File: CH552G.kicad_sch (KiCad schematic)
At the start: 13 parts, among them SW1 SW_SPST, SW2 SW_SPST, SW3 SW_SPST, SW4 SW_SPST, SW5 SW_SPST, SW6 SW_SPST, U1 CH552G

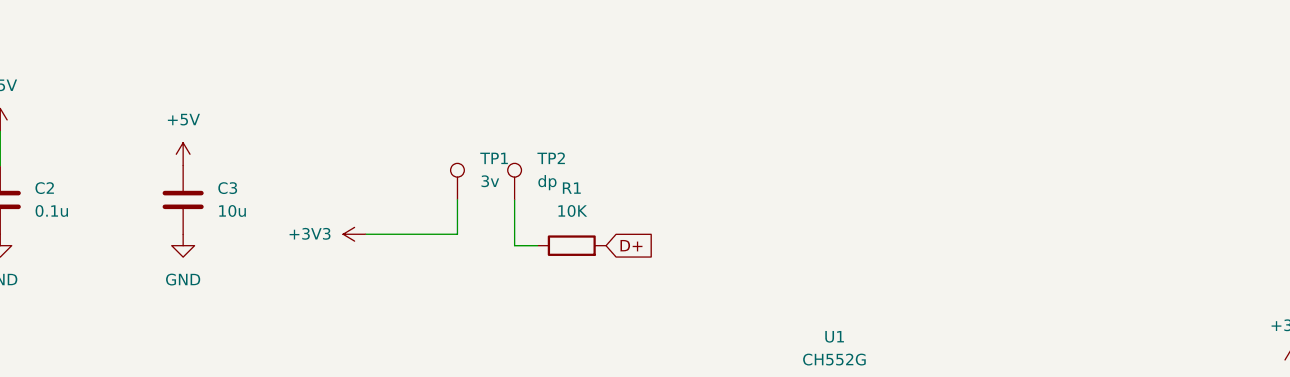
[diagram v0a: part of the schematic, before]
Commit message: updated titles and changes to wires
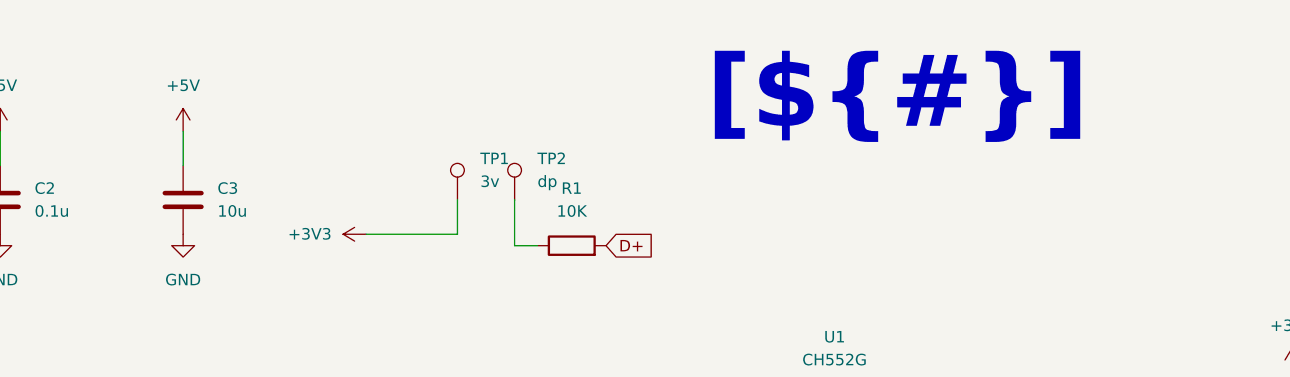
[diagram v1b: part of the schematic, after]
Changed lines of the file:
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@@
 	(generator_version "9.0")
 	(paper "A4")
+	(text_box "[${#}] ${TITLE}"
+		(exclude_from_sim no)
+		(at 82.55 16.002 0)
+		(size 130.81 12.7)
+		(margins 5.9999 5.9999 5.9999 5.9999)
+		(stroke
+			(width -0.0001)
+			(type default)
+		)
+		(fill
+			(type none)
+		)
+		(effects
+			(font
+				(face "Times New Roman")
+				(size 8 8)
+				(thickness 1.2)
+				(bold yes)
+				(color 162 22 34 1)
+			)
+		)
+	)
 	(junction
 		(at 35.56 27.94)
@@
 		(pts
 			(xy 40.64 135.89) (xy 54.61 135.89)
+		)
+		(stroke
+			(width 0)
+			(type default)
+		)
+	)
+	(wire
+		(pts
+			(xy 68.58 26.67) (xy 68.58 30.48)
 		)
 		(stroke
@@
 	(symbol
 		(lib_id "power:+5V")
-		(at 68.58 30.48 0)
+		(at 68.58 26.67 0)
 		(unit 1)
 		(exclude_from_sim no)
@@
 		(fields_autoplaced yes)
 		(property "Reference" "#PWR05"
-			(at 68.58 34.29 0)
+			(at 68.58 30.48 0)
 			(effects
 				(font
@@
 		)
 		(property "Value" "+5V"
-			(at 68.58 25.4 0)
+			(at 68.58 21.59 0)
 			(effects
 				(font
@@
 		)
 		(property "Footprint" ""
-			(at 68.58 30.48 0)
+			(at 68.58 26.67 0)
 			(effects
 				(font
@@
 		)
 		(property "Datasheet" ""
-			(at 68.58 30.48 0)
+			(at 68.58 26.67 0)
 			(effects
 				(font
@@
 		)
 		(property "Description" "Power symbol creates a global label with name \"+5V\""
-			(at 68.58 30.48 0)
-			(effects
-				(font
+			(at 68.58 26.67 0)
+			(effects
+				(font

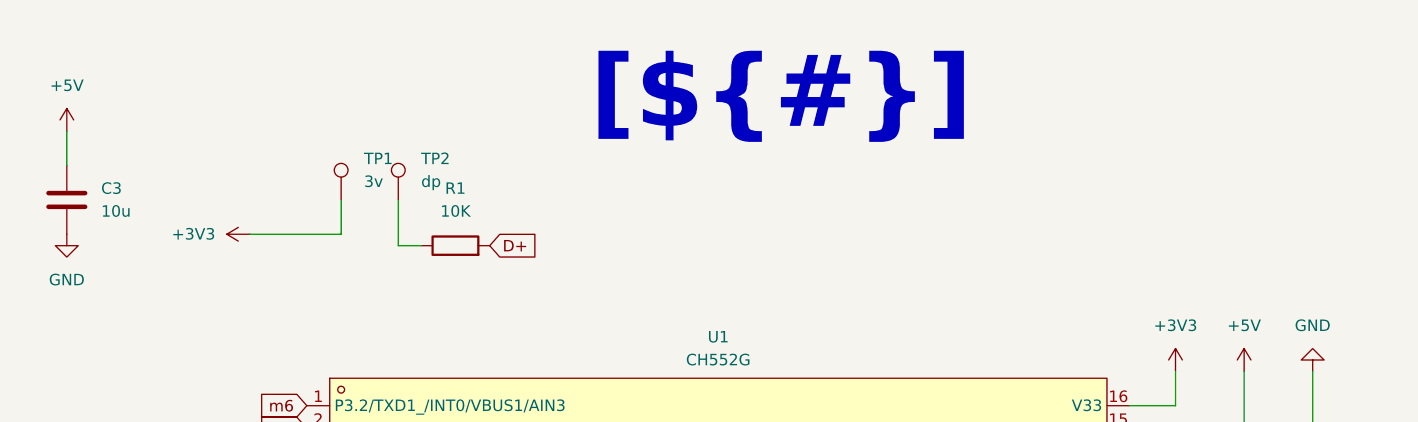
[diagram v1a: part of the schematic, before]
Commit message: updated titles and changes to wires
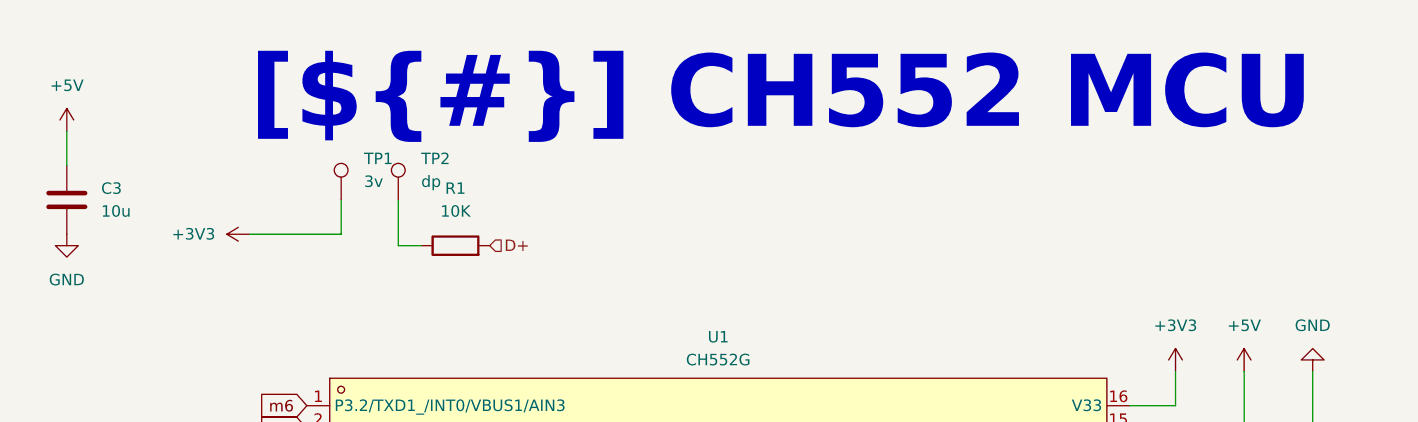
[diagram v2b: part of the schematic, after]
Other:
- title: (none) -> CH552 MCU
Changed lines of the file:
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@@
 	(generator_version "9.0")
 	(paper "A4")
+	(title_block
+		(title "CH552 MCU")
+	)
 	(text_box "[${#}] ${TITLE}"
 		(exclude_from_sim no)
@@
 		)
 	)
-	(global_label "D+"
+	(global_label "m1"
+		(shape input)
+		(at 95.25 72.39 180)
+		(fields_autoplaced yes)
+		(effects
+			(font
+				(size 1.27 1.27)
+			)
+			(justify right)
+		)
+		(property "Intersheetrefs" "${INTERSHEET_REFS}"
+			(at 89.362 72.39 0)
+			(effects
+				(font
+					(size 1.27 1.27)
+				)
+				(justify right)
+				(hide yes)
+			)
+		)
+	)
+	(global_label "m2"
+		(shape input)
+		(at 95.25 67.31 180)
+		(fields_autoplaced yes)
+		(effects
+			(font
+				(size 1.27 1.27)
+			)
+			(justify right)
+		)
+		(property "Intersheetrefs" "${INTERSHEET_REFS}"
+			(at 89.362 67.31 0)
+			(effects
+				(font
+					(size 1.27 1.27)
+				)
+				(justify right)
+				(hide yes)
+			)
+		)
+	)
+	(global_label "m4"
+		(shape input)
+		(at 95.25 62.23 180)
+		(fields_autoplaced yes)
+		(effects
+			(font
+				(size 1.27 1.27)
+			)
+			(justify right)
+		)
+		(property "Intersheetrefs" "${INTERSHEET_REFS}"
+			(at 89.362 62.23 0)
+			(effects
+				(font
+					(size 1.27 1.27)
+				)
+				(justify right)
+				(hide yes)
+			)
+		)
+	)
+	(global_label "m3"
+		(shape input)
+		(at 95.25 64.77 180)
+		(fields_autoplaced yes)
+		(effects
+			(font
+				(size 1.27 1.27)
+			)
+			(justify right)
+		)
+		(property "Intersheetrefs" "${INTERSHEET_REFS}"
+			(at 89.362 64.77 0)
+			(effects
+				(font
+					(size 1.27 1.27)
+				)
+				(justify right)
+				(hide yes)
+			)
+		)
+	)
+	(global_label "m6"
+		(shape input)
+		(at 95.25 57.15 180)
+		(fields_autoplaced yes)
+		(effects
+			(font
+				(size 1.27 1.27)
+			)
+			(justify right)
+		)
+		(property "Intersheetrefs" "${INTERSHEET_REFS}"
+			(at 89.362 57.15 0)
+			(effects
+				(font
+					(size 1.27 1.27)
+				)
+				(justify right)
+				(hide yes)
+			)
+		)
+	)
+	(global_label "m4"
+		(shape input)
+		(at 68.58 125.73 90)
+		(fields_autoplaced yes)
+		(effects
+			(font
+				(size 1.27 1.27)
+			)
+			(justify left)
+		)
+		(property "Intersheetrefs" "${INTERSHEET_REFS}"
+			(at 68.58 119.842 90)
+			(effects
+				(font
+					(size 1.27 1.27)
+				)
+				(justify left)
+				(hide yes)
+			)
+		)
+	)
+	(global_label "m1"
+		(shape input)
+		(at 26.67 125.73 90)
+		(fields_autoplaced yes)
+		(effects
+			(font
+				(size 1.27 1.27)
+			)
+			(justify left)
+		)
+		(property "Intersheetrefs" "${INTERSHEET_REFS}"
+			(at 26.67 119.842 90)
+			(effects
+				(font
+					(size 1.27 1.27)
+				)
+				(justify left)
+				(hide yes)
+			)
+		)
+	)
+	(global_label "m3"
+		(shape input)
+		(at 54.61 125.73 90)
+		(fields_autoplaced yes)
+		(effects
+			(font
+				(size 1.27 1.27)
+			)
+			(justify left)
+		)
+		(property "Intersheetrefs" "${INTERSHEET_REFS}"
+			(at 54.61 119.842 90)
+			(effects
+				(font
+					(size 1.27 1.27)
+				)
+				(justify left)
+				(hide yes)
+			)
+		)
+	)
+	(global_label "m5"
+		(shape input)
+		(at 82.55 125.73 90)
+		(fields_autoplaced yes)
+		(effects
+			(font
+				(size 1.27 1.27)
+			)
+			(justify left)
+		)
+		(property "Intersheetrefs" "${INTERSHEET_REFS}"
+			(at 82.55 119.842 90)
+			(effects
+				(font
+					(size 1.27 1.27)
+				)
+				(justify left)
+				(hide yes)
+			)
+		)
+	)
+	(global_label "m2"
+		(shape input)
+		(at 40.64 125.73 90)
+		(fields_autoplaced yes)
+		(effects
+			(font
+				(size 1.27 1.27)
+			)
+			(justify left)
+		)
+		(property "Intersheetrefs" "${INTERSHEET_REFS}"
+			(at 40.64 119.842 90)
+			(effects
+				(font
+					(size 1.27 1.27)
+				)
+				(justify left)
+				(hide yes)
+			)
+		)
+	)
+	(hierarchical_label "D-"
+		(shape input)
+		(at 186.69 67.31 0)
+		(effects
+			(font
+				(size 1.27 1.27)
+			)
+			(justify left)
+		)
+	)
+	(hierarchical_label "D+"
 		(shape input)
 		(at 115.57 39.37 0)
-		(fields_autoplaced yes)
-		(effects
-			(font
-				(size 1.27 1.27)
-			)
-			(justify left)
-		)
-		(property "Intersheetrefs" "${INTERSHEET_REFS}"
-			(at 121.3976 39.37 0)
-			(effects
-				(font
-					(size 1.27 1.27)
-				)
-				(justify left)
-				(hide yes)
-			)
-		)
-	)
-	(global_label "m1"
-		(shape input)
-		(at 95.25 72.39 180)
-		(fields_autoplaced yes)
-		(effects
-			(font
-				(size 1.27 1.27)
-			)
-			(justify right)
-		)
-		(property "Intersheetrefs" "${INTERSHEET_REFS}"
-			(at 89.362 72.39 0)
-			(effects
-				(font
-					(size 1.27 1.27)
-				)
-				(justify right)
-				(hide yes)
-			)
-		)
-	)
-	(global_label "m2"
-		(shape input)
-		(at 95.25 67.31 180)
-		(fields_autoplaced yes)
-		(effects
-			(font
-				(size 1.27 1.27)
-			)
-			(justify right)
-		)
-		(property "Intersheetrefs" "${INTERSHEET_REFS}"
-			(at 89.362 67.31 0)
-			(effects
-				(font
-					(size 1.27 1.27)
-				)
-				(justify right)
-				(hide yes)
-			)
-		)
-	)
-	(global_label "m4"
-		(shape input)
-		(at 95.25 62.23 180)
-		(fields_autoplaced yes)
-		(effects
-			(font
-				(size 1.27 1.27)
-			)
-			(justify right)
-		)
-		(property "Intersheetrefs" "${INTERSHEET_REFS}"
-			(at 89.362 62.23 0)
-			(effects
-				(font
-					(size 1.27 1.27)
-				)
-				(justify right)
-				(hide yes)
-			)
-		)
-	)
-	(global_label "m3"
-		(shape input)
-		(at 95.25 64.77 180)
-		(fields_autoplaced yes)
-		(effects
-			(font
-				(size 1.27 1.27)
-			)
-			(justify right)
-		)
-		(property "Intersheetrefs" "${INTERSHEET_REFS}"
-			(at 89.362 64.77 0)
-			(effects
-				(font
-					(size 1.27 1.27)
-				)
-				(justify right)
-				(hide yes)
-			)
-		)
-	)
-	(global_label "m6"
-		(shape input)
-		(at 95.25 57.15 180)
-		(fields_autoplaced yes)
-		(effects
-			(font
-				(size 1.27 1.27)
-			)
-			(justify right)
-		)
-		(property "Intersheetrefs" "${INTERSHEET_REFS}"
-			(at 89.362 57.15 0)
-			(effects
-				(font
-					(size 1.27 1.27)
-				)
-				(justify right)
-				(hide yes)
-			)
-		)
-	)
-	(global_label "m4"
-		(shape input)
-		(at 68.58 125.73 90)
-		(fields_autoplaced yes)
-		(effects
-			(font
-				(size 1.27 1.27)
-			)
-			(justify left)
-		)
-		(property "Intersheetrefs" "${INTERSHEET_REFS}"
-			(at 68.58 119.842 90)
-			(effects
-				(font
-					(size 1.27 1.27)
-				)
-				(justify left)
-				(hide yes)
-			)
-		)
-	)
-	(global_label "m1"
-		(shape input)
-		(at 26.67 125.73 90)
-		(fields_autoplaced yes)
-		(effects
-			(font
-				(size 1.27 1.27)
-			)
-			(justify left)
-		)
-		(property "Intersheetrefs" "${INTERSHEET_REFS}"
-			(at 26.67 119.842 90)
-			(effects
-				(font
-					(size 1.27 1.27)
-				)
-				(justify left)
-				(hide yes)
-			)
-		)
-	)
-	(global_label "m3"
-		(shape input)
-		(at 54.61 125.73 90)
-		(fields_autoplaced yes)
-		(effects
-			(font
-				(size 1.27 1.27)
-			)
-			(justify left)
-		)
-		(property "Intersheetrefs" "${INTERSHEET_REFS}"
-			(at 54.61 119.842 90)
-			(effects
-				(font
-					(size 1.27 1.27)
-				)
-				(justify left)
-				(hide yes)
-			)
-		)
-	)
-	(global_label "m5"
-		(shape input)
-		(at 82.55 125.73 90)
-		(fields_autoplaced yes)
-		(effects
-			(font
-				(size 1.27 1.27)
-			)
-			(justify left)
-		)
-		(property "Intersheetrefs" "${INTERSHEET_REFS}"
-			(at 82.55 119.842 90)
-			(effects
-				(font
-					(size 1.27 1.27)
-				)
-				(justify left)
-				(hide yes)
-			)
-		)
-	)
-	(global_label "m2"
-		(shape input)
-		(at 40.64 125.73 90)
-		(fields_autoplaced yes)
-		(effects
-			(font
-				(size 1.27 1.27)
-			)
-			(justify left)
-		)
-		(property "Intersheetrefs" "${INTERSHEET_REFS}"
-			(at 40.64 119.842 90)
-			(effects
-				(font
-					(size 1.27 1.27)
-				)
-				(justify left)
-				(hide yes)
-			)
-		)
-	)
-	(hierarchical_label "D-"
-		(shape input)
-		(at 186.69 67.31 0)
-		(effects
-			(font
+		(effects
+			(font
